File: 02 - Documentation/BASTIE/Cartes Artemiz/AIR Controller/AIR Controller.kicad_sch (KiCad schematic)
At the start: 24 parts, among them J1 3P Droit 22-11-2032, J4 2P Droit 2-11-2022, K2 Relais PCB, Q1 NMOS SQ2348ES-T1_GE3, U1 Alim LP TSR_0.5-2450, U4 Opamp_Dual, U5 ${SIM.PARAMS}

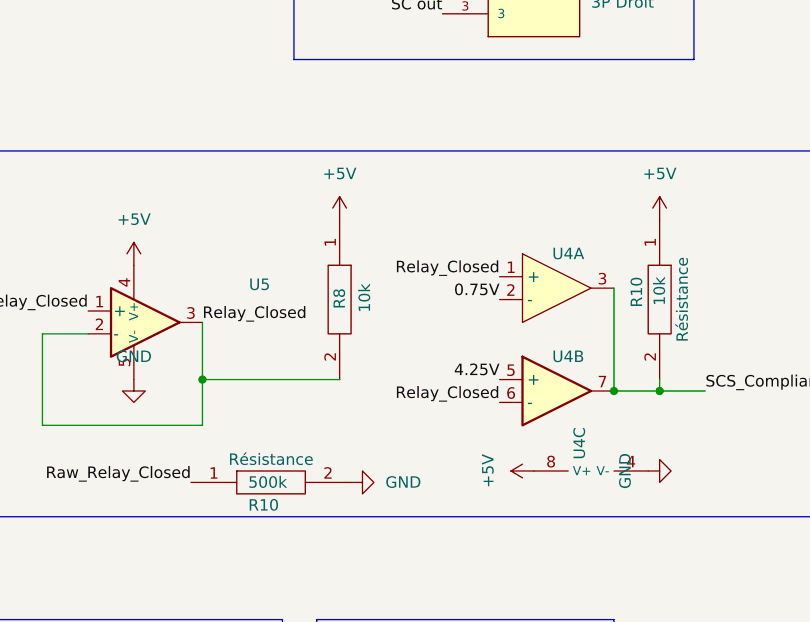
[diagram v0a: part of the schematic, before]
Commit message: Modifications cartes
Prise en compte des retours ECT + PCBs
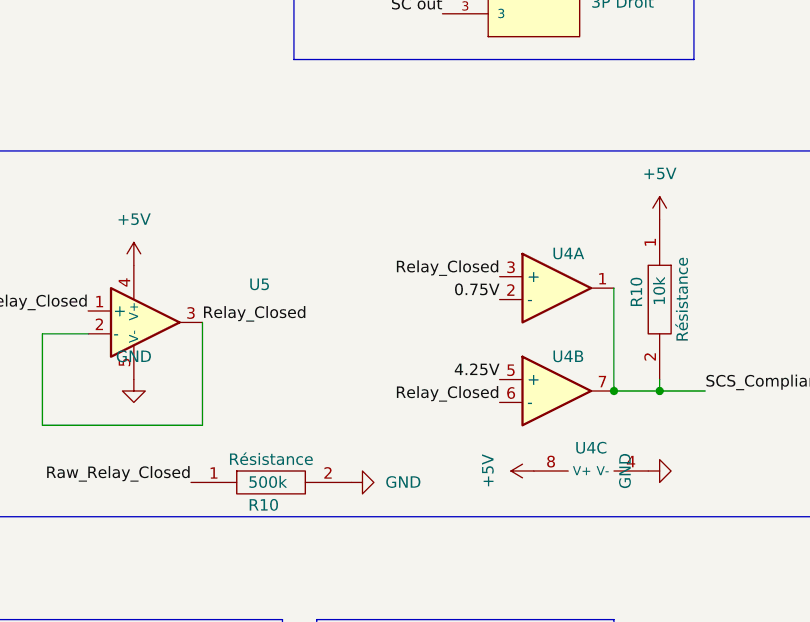
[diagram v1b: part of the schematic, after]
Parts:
- removed R8: 10k, EPSA_lib:RESC3216X70N, symbol EPSA_Lib:Résistance RK73H2BLTDD2152F
- U4: symbol EPSA_lib:Opamp_Dual -> EPSA_Lib:Comparator_Dual; Manufacturer_Part_Number TLV9062QPWRQ1 -> LMV393IPWR; Mouser Part Number 595-TLV9062QPWRQ1 -> 595-LMV393IPWR
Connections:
- net Relay_Closed: now also U4.3 (+); no longer U4.1 (+)
- net SCS_Compliance: now also U4.1; no longer U4.3
